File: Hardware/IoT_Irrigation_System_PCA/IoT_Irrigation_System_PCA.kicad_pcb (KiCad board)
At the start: 2 copper layers, 72.9 x 84 mm, 19 parts, among them J1 Conn_01x19_Socket, J2 Conn_01x19_Socket, J3 Conn_01x04_Socket, J4 691137710002, J5 691137710002, J6 691137710002, J7 Jack-DC, Q1 IRLZ34N, U1 LM2575-5.0BT

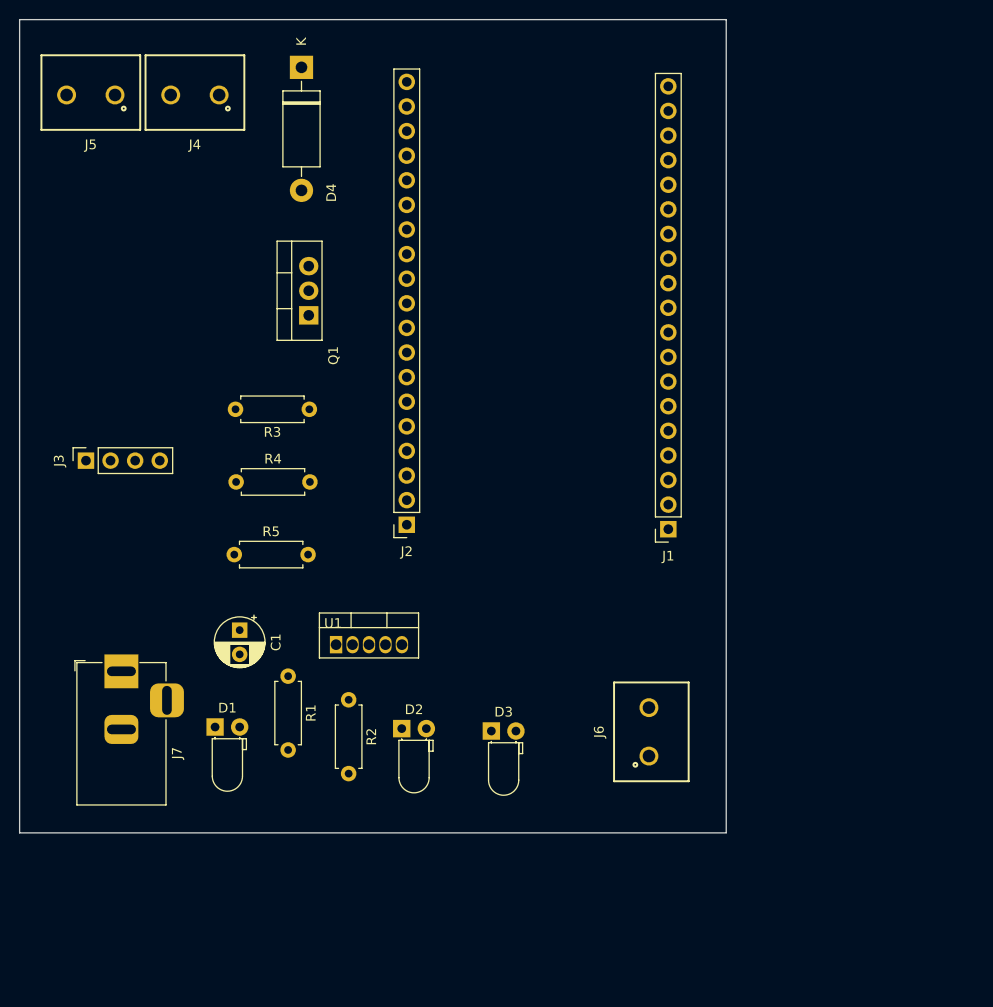
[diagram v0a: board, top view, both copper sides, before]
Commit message: 1. Added Wifi connectivity logic 2. Fixed error in getSettings() tries loop 3. Modified TB delay to 180s (3 min) 4. Updates to PCB design
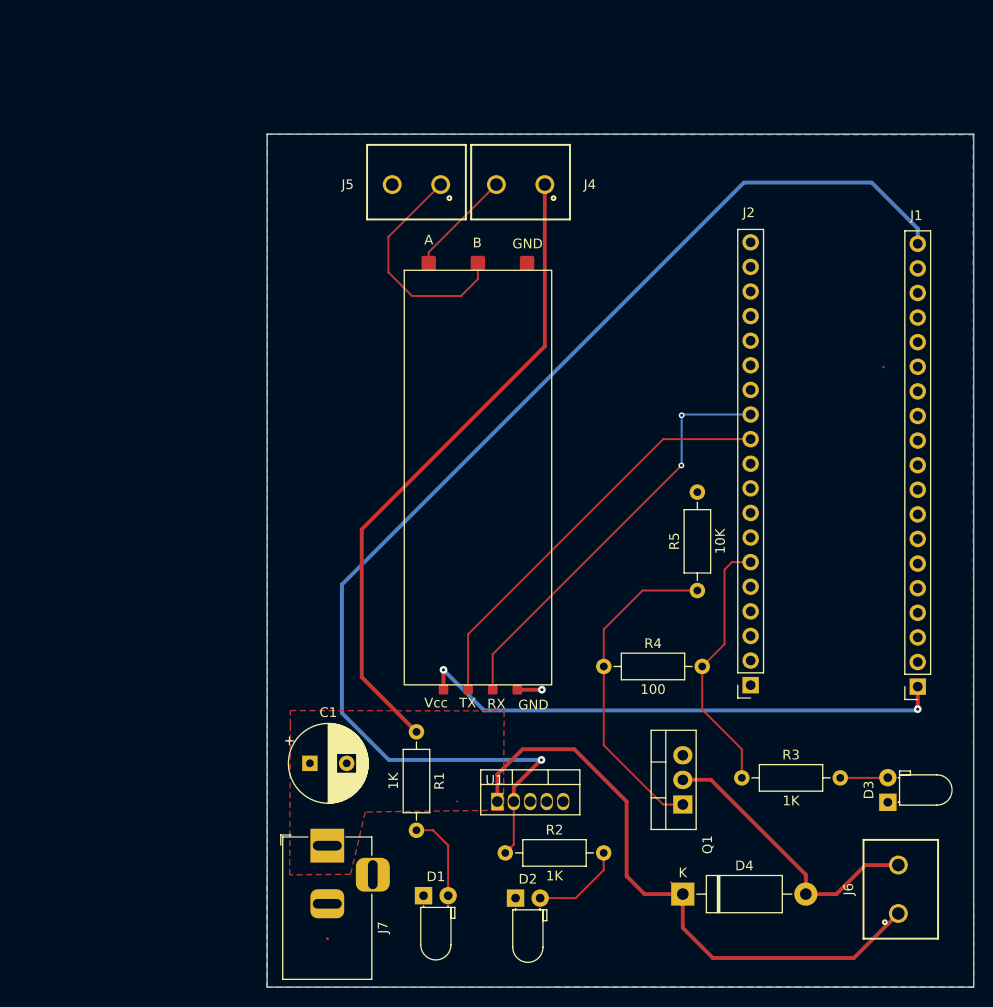
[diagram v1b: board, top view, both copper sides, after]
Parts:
- C1: footprint Capacitor_THT:CP_Radial_D5.0mm_P2.50mm -> Capacitor_THT:CP_Radial_D8.0mm_P3.80mm
- J3: value Conn_01x04_Socket -> RS485_Module; footprint Connector_PinSocket_2.54mm:PinSocket_1x04_P2.54mm_Vertical -> RS485_Module:HW-519R4
- R1, R2, R3, R4, R5: footprint Resistor_THT:R_Axial_DIN0207_L6.3mm_D2.5mm_P7.62mm_Horizontal -> Resistor_THT:R_Axial_DIN0207_L6.3mm_D2.5mm_P10.16mm_Horizontal
- moved D4 94.0 mm to (155.5, 133.8), turned to 0 degrees
- moved Q1 63.6 mm to (155.5, 124.5)
- moved R3 58.7 mm to (161.6, 121.8), turned to 0 degrees
- moved R5 48.0 mm to (157.0, 102.4), turned to 90 degrees
- moved R4 42.5 mm to (147.3, 110.2)
- moved D3 41.6 mm to (176.7, 124.3), turned to 90 degrees
- moved J2 39.2 mm to (162.5, 112.2)
- moved J3 38.3 mm to (126.7, 69.3), turned to 0 degrees
- moved J4 34.9 mm to (138.8, 60.5)
- moved J5 34.9 mm to (128.0, 60.5)
- moved J1 30.4 mm to (179.8, 112.3)
- moved J6 30.4 mm to (177.8, 133.2)
- moved J7 27.8 mm to (118.8, 128.8)
- moved D1 27.7 mm to (128.7, 133.9)
- moved U1 23.2 mm to (136.3, 124.2)
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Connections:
- J3 pad 2: /RS485_TX -> /RS485_A
- J3 pad 3: /RS485_RX -> /RS485_TX
- J3 pad 4: GND -> /RS485_B
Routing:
- net /PWR_IN: track 0.00 -> 131.1 mm
- net /+5VDC: track 0.00 -> 127.2 mm, vias 0 -> 1
- net /+3p3VDC: track 0.00 -> 55.2 mm, vias 0 -> 2
- net /RS485_RX: track 0.00 -> 43.6 mm, vias 0 -> 2
- net /RS485_TX: track 0.00 -> 43.2 mm
- net Net-(Q1-G): track 0.00 -> 34.0 mm
- net Net-(D4-A): track 0.00 -> 29.6 mm
- net /SOLENOID_CTRL: track 0.00 -> 27.2 mm
- net /RS485_B: track 0.00 -> 23.9 mm
- net /RS485_A: track 0.00 -> 11.0 mm
- net Net-(D2-A): track 0.00 -> 9.53 mm
- net Net-(D1-A): track 0.00 -> 9.14 mm
- net Net-(D3-A): track 0.00 -> 4.92 mm
- net GND: track 0.00 -> 2.75 mm, vias 0 -> 1
- added copper zone on F.Cu, net /PWR_IN
- added copper zone on B.Cu, net GND
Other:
- board size 72.9 x 84 mm -> 73 x 88.1 mm
- board text added: "A"
- board text added: "B"
- board text added: "GND"
- board text added: "RX"
- board text added: "TX"
- board text added: "Vcc"

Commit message: Updated PCB
Spaced ESP32 socket headers to 25.4mm
Moved RS485 and power supply components
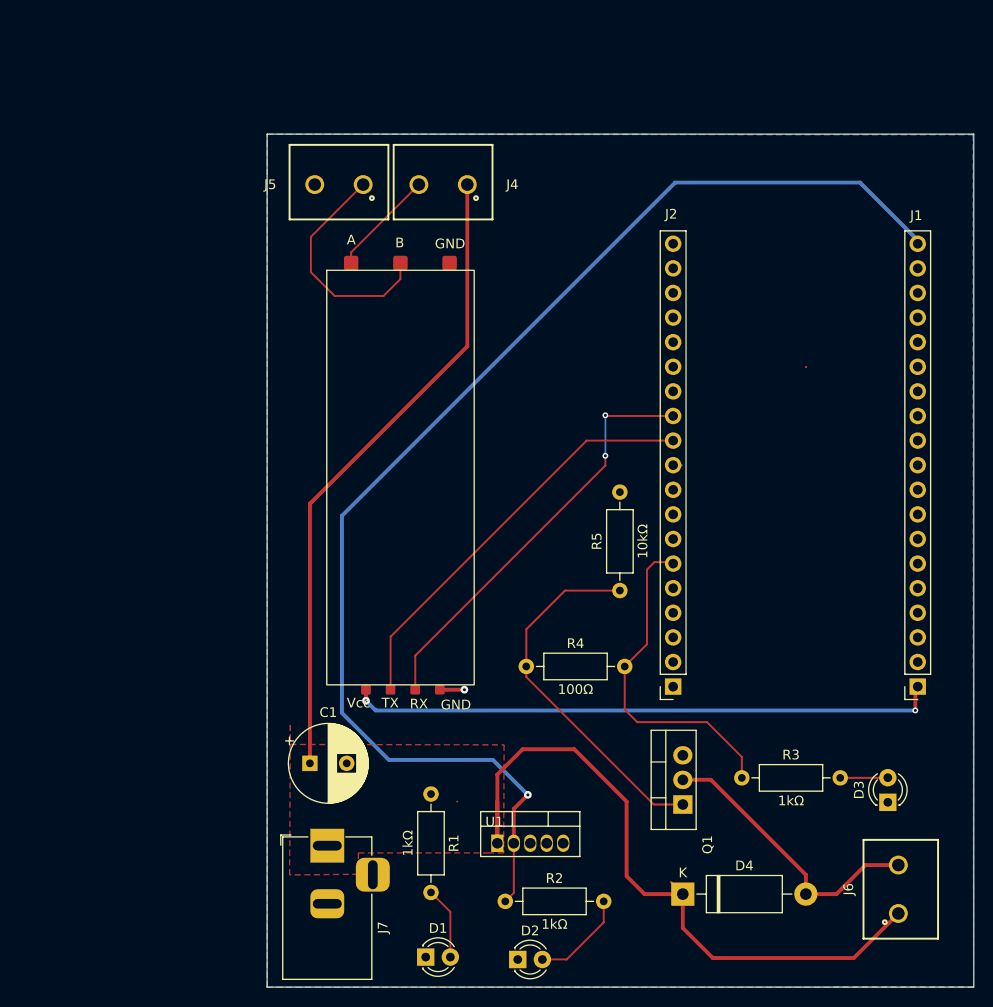
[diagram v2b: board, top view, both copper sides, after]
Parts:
- C1: value C_Polarized -> 100µF
- D1, D2, D3: footprint LED_THT:LED_D3.0mm_Horizontal_O1.27mm_Z2.0mm -> LED_THT:LED_D3.0mm
- J3: value RS485_Module -> HW-519R4
- R1, R2, R3: value 1K -> 1kΩ
- R4: value 100 -> 100Ω
- R5: value 10K -> 10kΩ
- moved J2 8.00 mm to (154.5, 112.3)
- moved J3 8.00 mm to (118.7, 69.3)
- moved J4 8.00 mm to (130.8, 60.5)
- moved J5 8.00 mm to (120.0, 60.5)
- moved R4 8.00 mm to (139.3, 110.2)
- moved R5 8.00 mm to (149.0, 102.4)
- moved R1 6.59 mm to (129.5, 123.4)
- moved D1 6.34 mm to (129.0, 140.2)
- moved D2 6.34 mm to (138.5, 140.5)
- moved R2 5.00 mm to (137.2, 134.5)
- moved U1 4.31 mm to (136.3, 128.5)
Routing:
- net /PWR_IN: track 131.1 -> 139.5 mm
- net /SOLENOID_CTRL: track 27.2 -> 34.7 mm
- net /+3p3VDC: track 55.2 -> 60.8 mm
- net /+5VDC: track 127.2 -> 131.7 mm
- net Net-(Q1-G): track 34.0 -> 37.9 mm
- net Net-(D1-A): track 9.14 -> 7.50 mm
- net Net-(D2-A): track 9.53 -> 10.1 mm

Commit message: 1.Added LittleFS to store TB settings 2. Moved functions from thingspeak to helper file 3. Modified setting structure to store TB values 4. Added precompiler directives to allow for no soil sensor and debbie's location
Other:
- board text added: "GIZMO LTD IoT Irrigation Control and Soil Monitoring System ver 1.0 Jan 2026"
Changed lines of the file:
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@@
+		)
+	)
+	(gr_text "GIZMO LTD\nIoT Irrigation Control\nand Soil Monitoring System\nver 1.0\nJan 2026"
+		(at 163 100.5 270)
+		(layer "B.SilkS")
+		(effects
+			(font
+				(size 1 1)
+				(thickness 0.1)
+			)
+			(justify left bottom mirror)
 		)
 	)
